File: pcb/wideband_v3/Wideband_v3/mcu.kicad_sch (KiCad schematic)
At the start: 44 parts, among them J1 Conn_01x14, J2 USB_C_Receptacle_USB2.0, J3 Tag connect, SW1 Key0, SW3 Key1, U1 RP2040, U2 W25Q128JVS, U8 AMS1117-3.3, Y1 12MHz

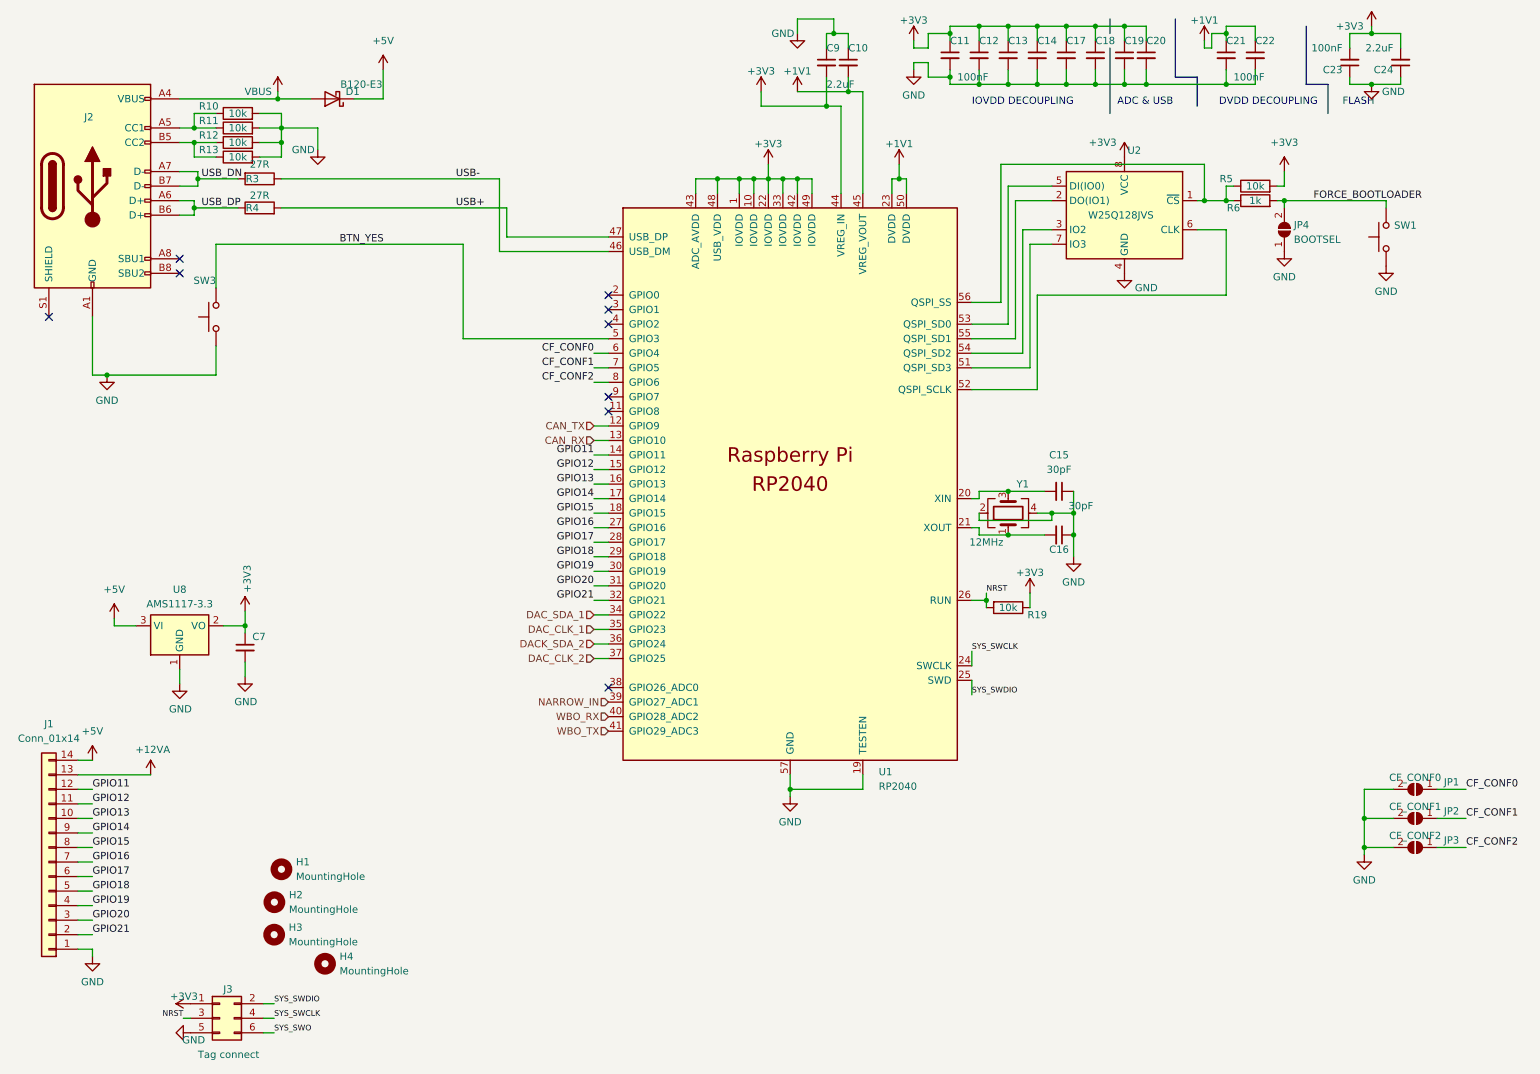
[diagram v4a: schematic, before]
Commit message: update LCSC/Stock codes, update pcb to new footprints
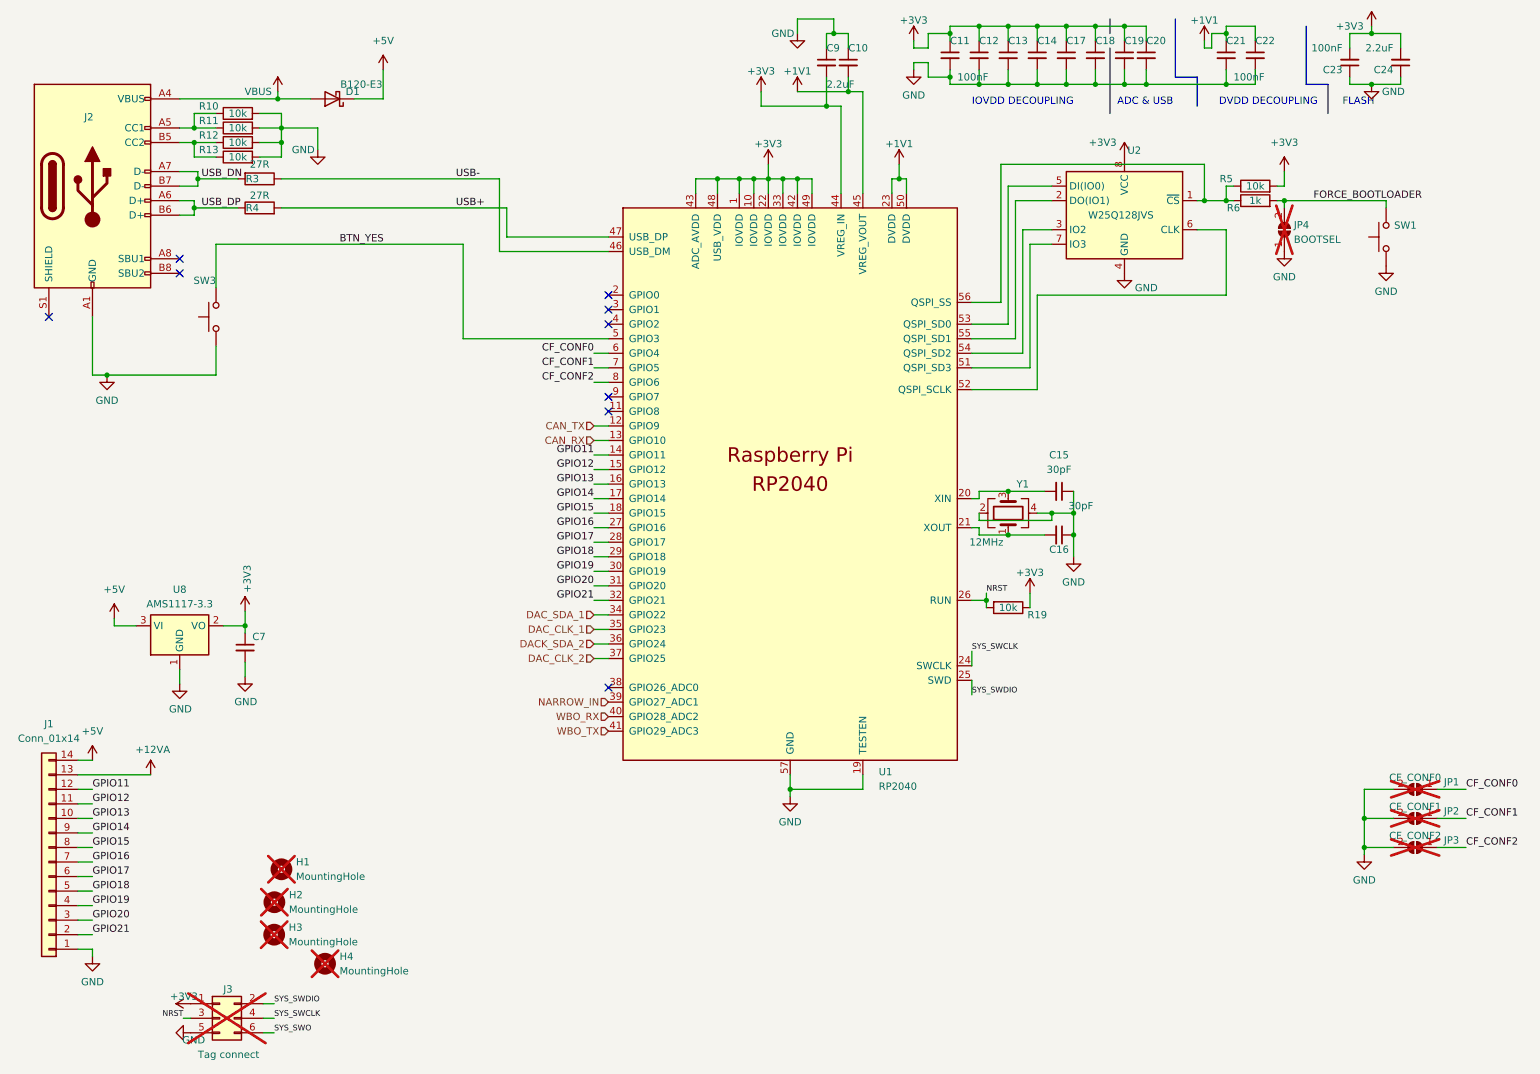
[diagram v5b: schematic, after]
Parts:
- C10, C24, C9: footprint Capacitor_SMD:C_0603_1608Metric -> Capacitor_SMD:C_0805_2012Metric; LCSC (none) -> C49217; STOCK (none) -> CAP-000176-00
- C11, C12, C13, C14, C17, C18, C19, C20, C21, C22, C23: LCSC (none) -> C14663; STOCK (none) -> CAP-000062-00
- C15, C16: LCSC (none) -> C18164620; STOCK (none) -> CAP-000396-00
- C7: footprint Capacitor_SMD:C_0805_2012Metric -> Capacitor_SMD:C_0603_1608Metric; LCSC C49678 -> C14663; STOCK (none) -> CAP-000062-00
- D1: LCSC (none) -> C84343; STOCK (none) -> DIO-000134-00
- H1, H2, H3, H4, J3, JP1, JP2, JP3, JP4: LCSC (none) -> -; STOCK (none) -> -; now not fitted
- J1: LCSC (none) -> C7494795; STOCK (none) -> CON-000409-00
- J2: STOCK (none) -> CON-000399-00
- R10, R11, R12, R13, R19, R5: LCSC (none) -> C115324; STOCK (none) -> RES-000118-00
- R3, R4: LCSC (none) -> C25190; STOCK (none) -> RES-000240-00
- R6: LCSC (none) -> C21190; STOCK (none) -> RES-000107-00
- SW1: LCSC (none) -> C412370; STOCK (none) -> MEC-000125-00
- SW3: LCSC (none) -> C2798927; STOCK (none) -> MEC-000039-00
- U1: LCSC (none) -> C2040; STOCK (none) -> ICS-000014-00
- U2: LCSC (none) -> C97521; STOCK (none) -> ICS-000404-00
- U8: LCSC (none) -> C6186; STOCK (none) -> PWR-000102-00
- Y1: STOCK (none) -> CLK-000282-00
